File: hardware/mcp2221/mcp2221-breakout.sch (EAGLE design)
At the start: 8 parts, among them IC2 LD33V, U3 MCP2221-I/SL, X1 USBPTH

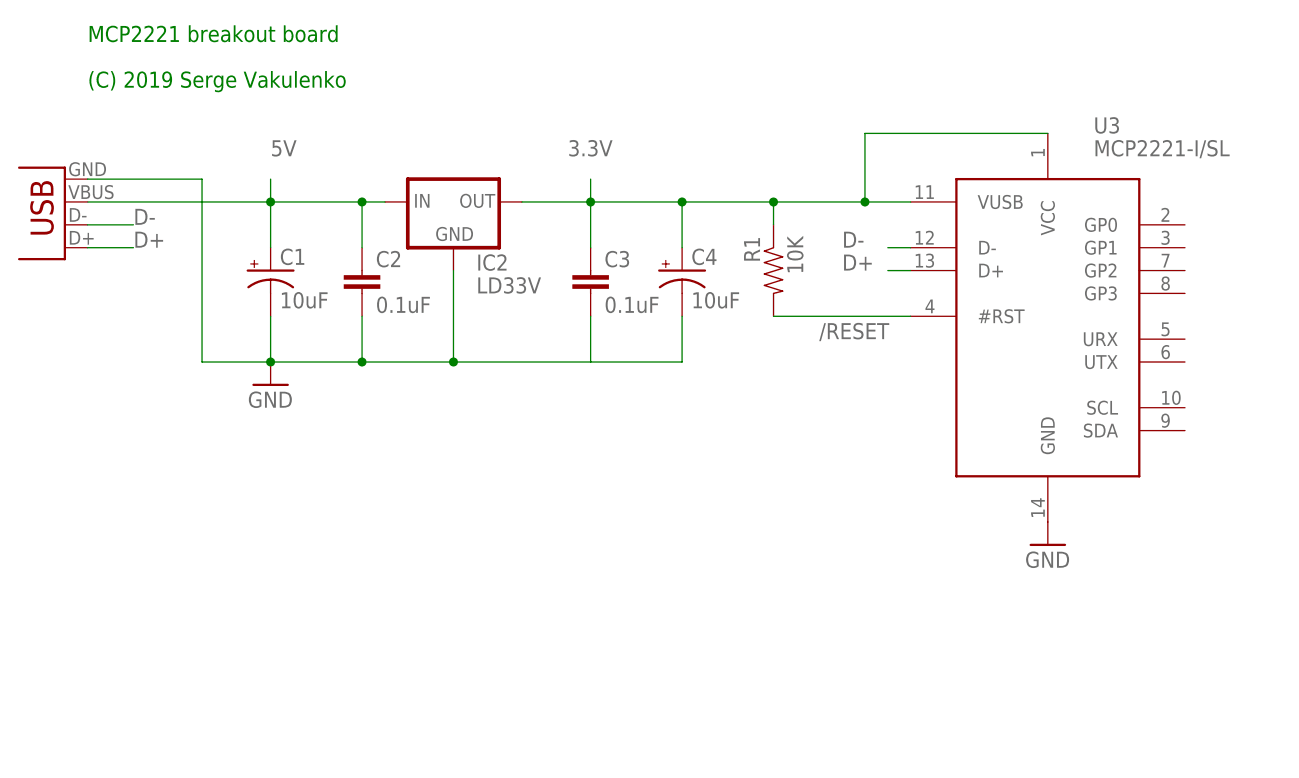
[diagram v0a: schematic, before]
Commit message: Update mcp2221 schematic.
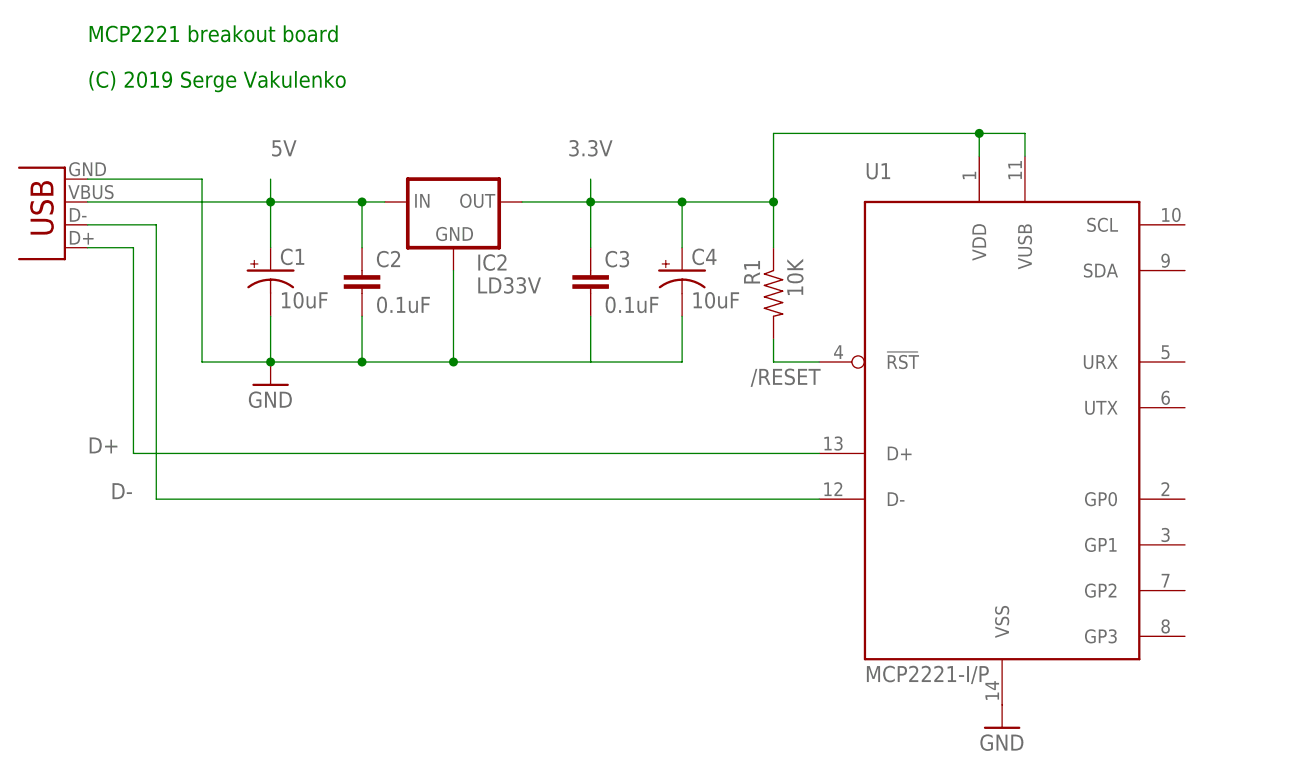
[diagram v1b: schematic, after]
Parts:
- removed U3: MCP2221-I/SL, ak:MCP2221-I/SL
- added U1: MCP2221-I/P, microchip-mcp2221:MCP2221-I/P
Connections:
- net /RESET: now also U1.!RST; no longer U3.#RST
- net 3.3V: now also U1.VDD, U1.VUSB; no longer U3.VCC, U3.VUSB
- net D+: now also U1.D+; no longer U3.D+
- net D-: now also U1.D-; no longer U3.D-
- net GND: now also U1.VSS; no longer U3.GND
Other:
- moved on the sheet: R1
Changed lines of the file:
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@@
 <layer number="54" name="bGND_GNDA" color="1" fill="9" visible="yes" active="no"/>
 <layer number="56" name="wert" color="7" fill="1" visible="yes" active="no"/>
-<layer number="57" name="tCAD" color="7" fill="1" visible="no" active="no"/>
-<layer number="59" name="tCarbon" color="7" fill="1" visible="no" active="no"/>
-<layer number="60" name="bCarbon" color="7" fill="1" visible="no" active="no"/>
+<layer number="57" name="tCAD" color="7" fill="1" visible="yes" active="no"/>
+<layer number="59" name="tCarbon" color="7" fill="1" visible="yes" active="no"/>
+<layer number="60" name="bCarbon" color="7" fill="1" visible="yes" active="no"/>
 <layer number="90" name="Modules" color="5" fill="1" visible="yes" active="yes"/>
 <layer number="91" name="Nets" color="2" fill="1" visible="yes" active="yes"/>
@@
 <part name="C4" library="SparkFun" deviceset="CAP_POL" device="PTH2" value="10uF"/>
 <part name="R1" library="SparkFun" deviceset="RESISTOR" device="PTH1" value="10K"/>
-<part name="U3" library="ak" deviceset="MCP2221-I/SL" device=""/>
 <part name="GND2" library="supply1" deviceset="GND" device=""/>
+<part name="U1" library="microchip-mcp2221" deviceset="MCP2221-*" device="I/P"/>
 </parts>
 <sheets>
@@
 <instance part="GND1" gate="1" x="20.32" y="68.58"/>
 <instance part="C4" gate="G$1" x="66.04" y="81.28"/>
-<instance part="R1" gate="G$1" x="76.2" y="81.28" rot="MR270"/>
-<instance part="U3" gate="G$1" x="106.68" y="76.2"/>
-<instance part="GND2" gate="1" x="106.68" y="50.8"/>
+<instance part="R1" gate="G$1" x="76.2" y="78.74" rot="MR270"/>
+<instance part="GND2" gate="1" x="101.6" y="30.48"/>
+<instance part="U1" gate="G$1" x="101.6" y="63.5"/>
 </instances>
 <busses>
@@
 </segment>
 <segment>
-<pinref part="U3" gate="G$1" pin="GND"/>
+<pinref part="U1" gate="G$1" pin="VSS"/>
 <pinref part="GND2" gate="1" pin="GND"/>
 </segment>
@@
 <pinref part="C4" gate="G$1" pin="+"/>
 <pinref part="R1" gate="G$1" pin="1"/>
-<wire x1="76.2" y1="86.36" x2="76.2" y2="88.9" width="0.1524" layer="91"/>
+<wire x1="76.2" y1="83.82" x2="76.2" y2="88.9" width="0.1524" layer="91"/>
+<wire x1="76.2" y1="88.9" x2="76.2" y2="96.52" width="0.1524" layer="91"/>
+<pinref part="U1" gate="G$1" pin="VUSB"/>
+<wire x1="76.2" y1="96.52" x2="99.06" y2="96.52" width="0.1524" layer="91"/>
+<wire x1="99.06" y1="96.52" x2="104.14" y2="96.52" width="0.1524" layer="91"/>
+<wire x1="104.14" y1="96.52" x2="104.14" y2="93.98" width="0.1524" layer="91"/>
+<pinref part="U1" gate="G$1" pin="VDD"/>
+<wire x1="99.06" y1="96.52" x2="99.06" y2="93.98" width="0.1524" layer="91"/>
 <junction x="76.2" y="88.9"/>
-<pinref part="U3" gate="G$1" pin="VUSB"/>
-<wire x1="76.2" y1="88.9" x2="86.36" y2="88.9" width="0.1524" layer="91"/>
-<pinref part="U3" gate="G$1" pin="VCC"/>
-<wire x1="86.36" y1="88.9" x2="91.44" y2="88.9" width="0.1524" layer="91"/>
-<wire x1="106.68" y1="96.52" x2="86.36" y2="96.52" width="0.1524" layer="91"/>
-<wire x1="86.36" y1="96.52" x2="86.36" y2="88.9" width="0.1524" layer="91"/>
-<junction x="86.36" y="88.9"/>
+<junction x="99.06" y="96.52"/>
 </segment>
 </net>
 <net name="D-" class="0">
 <segment>
-<wire x1="0" y1="86.36" x2="5.08" y2="86.36" width="0.1524" layer="91"/>
-<label x="5.08" y="86.36" size="1.778" layer="95"/>
+<wire x1="0" y1="86.36" x2="7.62" y2="86.36" width="0.1524" layer="91"/>
 <pinref part="X1" gate="G$1" pin="D-"/>
-</segment>
-<segment>
-<pinref part="U3" gate="G$1" pin="D-"/>
-<wire x1="91.44" y1="83.82" x2="88.9" y2="83.82" width="0.1524" layer="91"/>
-<label x="83.82" y="83.82" size="1.778" layer="95"/>
+<wire x1="7.62" y1="86.36" x2="7.62" y2="55.88" width="0.1524" layer="91"/>
+<label x="2.54" y="55.88" size="1.778" layer="95"/>
+<pinref part="U1" gate="G$1" pin="D-"/>
+<wire x1="7.62" y1="55.88" x2="81.28" y2="55.88" width="0.1524" layer="91"/>
 </segment>
 </net>
@@
 <net name="D+" class="0">
 <segment>
+<label x="0" y="60.96" size="1.778" layer="95"/>
+<pinref part="U1" gate="G$1" pin="D+"/>
+<wire x1="81.28" y1="60.96" x2="5.08" y2="60.96" width="0.1524" layer="91"/>
 <wire x1="0" y1="83.82" x2="5.08" y2="83.82" width="0.1524" layer="91"/>
-<label x="5.08" y="83.82" size="1.778" layer="95"/>
 <pinref part="X1" gate="G$1" pin="D+"/>
-</segment>
-<segment>
-<pinref part="U3" gate="G$1" pin="D+"/>
-<wire x1="91.44" y1="81.28" x2="88.9" y2="81.28" width="0.1524" layer="91"/>
-<label x="83.82" y="81.28" size="1.778" layer="95"/>
+<wire x1="5.08" y1="60.96" x2="5.08" y2="83.82" width="0.1524" layer="91"/>
 </segment>
 </net>
 <net name="/RESET" class="0">
 <segment>
+<pinref part="U1" gate="G$1" pin="!RST"/>
+<wire x1="81.28" y1="71.12" x2="76.2" y2="71.12" width="0.1524" layer="91"/>
 <pinref part="R1" gate="G$1" pin="2"/>
-<pinref part="U3" gate="G$1" pin="#RST"/>
-<wire x1="76.2" y1="76.2" x2="91.44" y2="76.2" width="0.1524" layer="91"/>
-<label x="81.28" y="73.66" size="1.778" layer="95"/>
-</segment>
-</net>
+<wire x1="76.2" y1="71.12" x2="76.2" y2="73.66" width="0.1524" layer="91"/>
+<label x="73.66" y="68.58" size="1.778" layer="95"/>
+</segment>
+</net>
